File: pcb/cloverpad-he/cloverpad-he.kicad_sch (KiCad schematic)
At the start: 65 parts, among them J1 USB_C_Receptacle_USB2.0, SW1 SW_Push, SW2 SW_Push, U1 SRV05-4, U2 XC6206P332MR, U3 DRV5056A4xDBZxQ1, U4 DRV5056A4xDBZxQ1, U5 DRV5056A4xDBZxQ1, U6 74AHCT1G125, U7 74AHCT1G125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

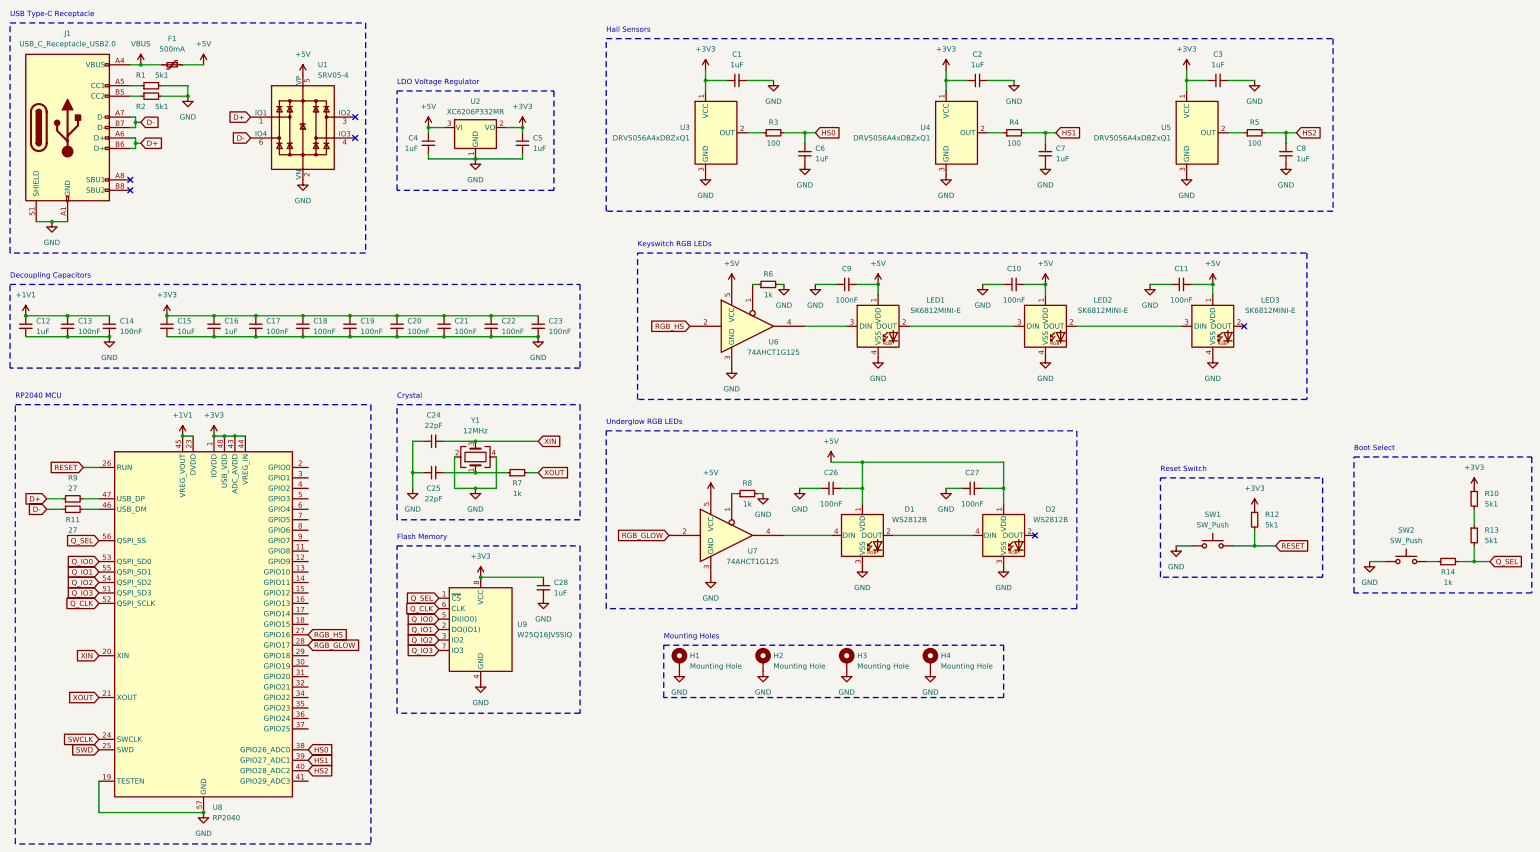
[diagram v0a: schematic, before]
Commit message: chore: remove rgb from Cloverpad HE pcb
I want to keep the cost down; including RGB means that standard PCB assembly is needed, which causes the price to spike...
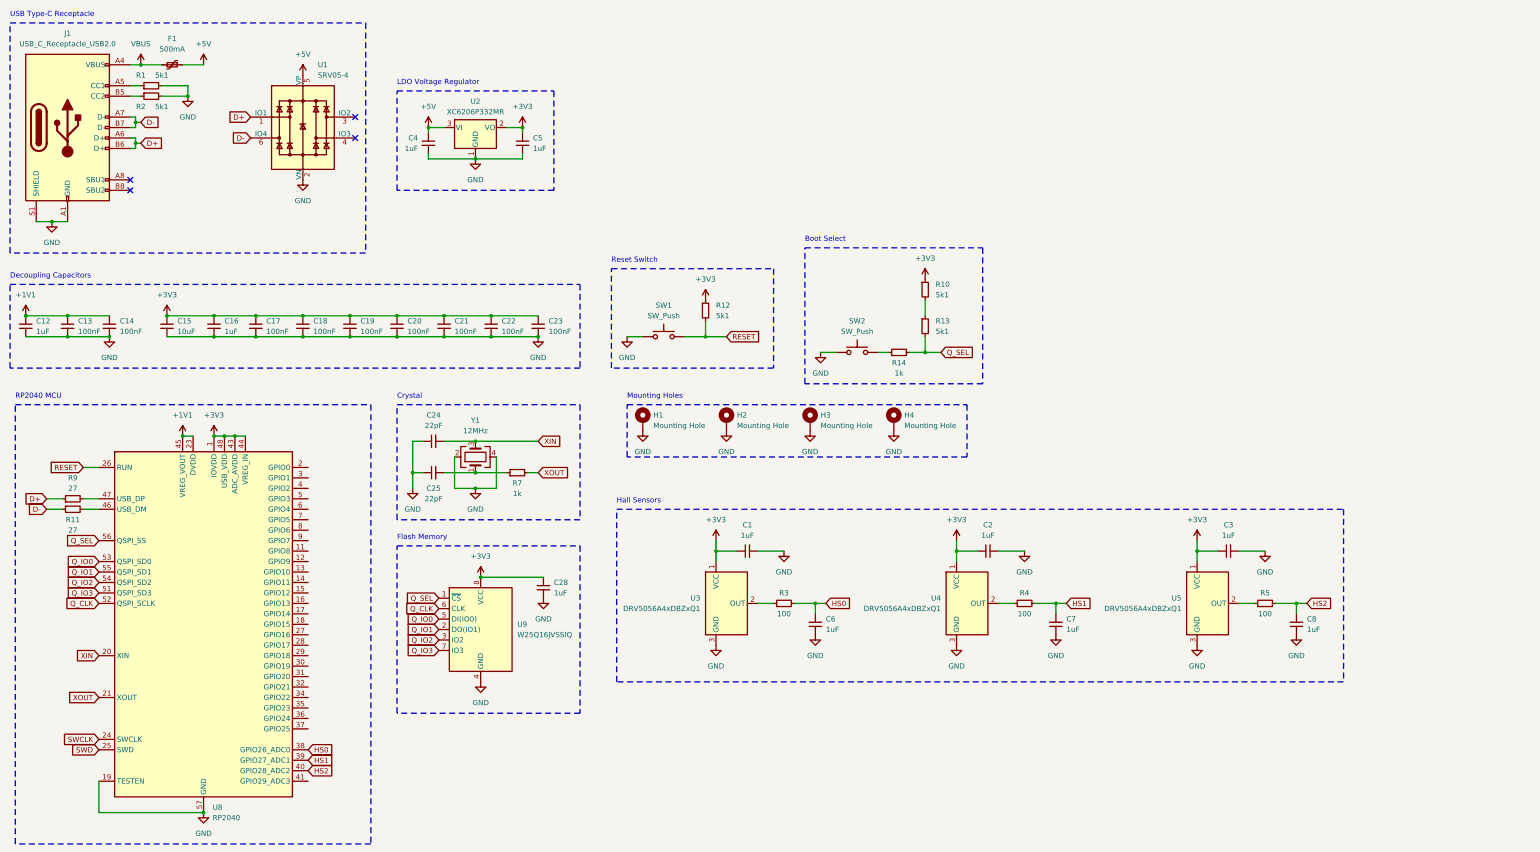
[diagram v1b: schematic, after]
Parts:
- removed C10, C11, C26, C27, C9: 100nF, Capacitor_SMD:C_0402_1005Metric, symbol Device:C_Small
- removed D1, D2: WS2812B, LED_SMD:LED_WS2812B_PLCC4_5.0x5.0mm_P3.2mm, symbol LED:WS2812B
- removed LED1, LED2, LED3: SK6812MINI-E, PCM_marbastlib-mx:LED_MX_6028R, symbol PCM_marbastlib-mx:MX_SK6812MINI-E
- removed R6, R8: 1k, Resistor_SMD:R_0402_1005Metric, symbol Device:R_Small
- removed U6, U7: 74AHCT1G125, Package_TO_SOT_SMD:SOT-353_SC-70-5, symbol 74xGxx:74AHCT1G125
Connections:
- net RGB_GLOW: no longer names the net of U8.28 (GPIO17)
- net RGB_HS: no longer names the net of U8.27 (GPIO16)
- no-connect marks 6 -> 4
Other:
- note removed: "Keyswitch RGB LEDs"
- note removed: "Underglow RGB LEDs"
- moved on the sheet: C1, C2, C3, C6, C7, C8, H1, H2, H3, H4, R10, R12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

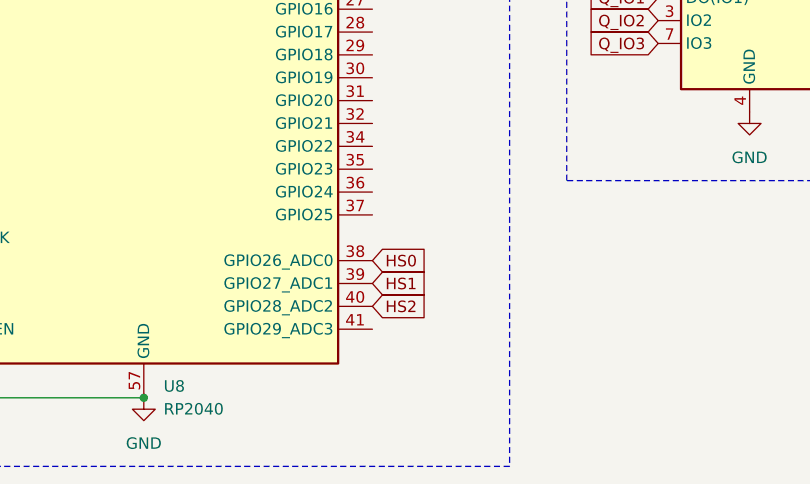
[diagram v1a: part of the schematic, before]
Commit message: fix: swap positions of HS0 and HS2 on cloverpad he
same as on cloverpad mx - this puts HS0 on the leftmost side.
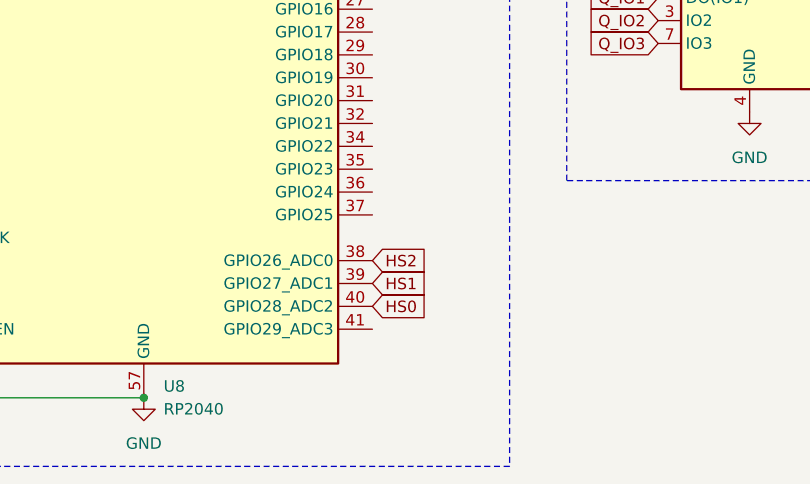
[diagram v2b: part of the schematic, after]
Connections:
- net HS0: now also U8.40 (GPIO28_ADC2); no longer U8.38 (GPIO26_ADC0)
- net HS2: now also U8.38 (GPIO26_ADC0); no longer U8.40 (GPIO28_ADC2)
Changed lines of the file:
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@@
     )
   )
-  (global_label "HS2" (shape input) (at 87.63 199.39 0) (fields_autoplaced)
+  (global_label "HS2" (shape input) (at 87.63 194.31 0) (fields_autoplaced)
     (effects (font (size 1.27 1.27)) (justify left))
-    (property "Intersheetrefs" "${INTERSHEET_REFS}" (at 94.3647 199.39 0)
+    (property "Intersheetrefs" "${INTERSHEET_REFS}" (at 94.3647 194.31 0)
       (effects (font (size 1.27 1.27)) (justify left) hide)
     )
@@
     )
   )
-  (global_label "HS0" (shape input) (at 87.63 194.31 0) (fields_autoplaced)
+  (global_label "HS0" (shape input) (at 87.63 199.39 0) (fields_autoplaced)
     (effects (font (size 1.27 1.27)) (justify left))
-    (property "Intersheetrefs" "${INTERSHEET_REFS}" (at 94.3647 194.31 0)
+    (property "Intersheetrefs" "${INTERSHEET_REFS}" (at 94.3647 199.39 0)
       (effects (font (size 1.27 1.27)) (justify left) hide)
     )

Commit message: fix: port pcb size changes to cloverpad he
since there's no RGB now, it's possible to route the analog signals more directly.
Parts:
- H1, H2, H3, H4: footprint MountingHole:MountingHole_3.5mm_Pad -> MountingHole:MountingHole_2.2mm_M2_Pad
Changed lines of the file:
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@@
       (effects (font (size 1.27 1.27)) (justify left))
     )
-    (property "Footprint" "MountingHole:MountingHole_3.5mm_Pad" (at 189.23 114.3 0)
+    (property "Footprint" "MountingHole:MountingHole_2.2mm_M2_Pad" (at 189.23 114.3 0)
       (effects (font (size 1.27 1.27)) hide)
     )
@@
       (effects (font (size 1.27 1.27)) (justify left))
     )
-    (property "Footprint" "MountingHole:MountingHole_3.5mm_Pad" (at 209.55 114.3 0)
+    (property "Footprint" "MountingHole:MountingHole_2.2mm_M2_Pad" (at 209.55 114.3 0)
       (effects (font (size 1.27 1.27)) hide)
     )
@@
       (effects (font (size 1.27 1.27)) (justify left))
     )
-    (property "Footprint" "MountingHole:MountingHole_3.5mm_Pad" (at 168.91 114.3 0)
+    (property "Footprint" "MountingHole:MountingHole_2.2mm_M2_Pad" (at 168.91 114.3 0)
       (effects (font (size 1.27 1.27)) hide)
     )
@@
       (effects (font (size 1.27 1.27)) (justify left))
     )
-    (property "Footprint" "MountingHole:MountingHole_3.5mm_Pad" (at 229.87 114.3 0)
-      (effects (font (size 1.27 1.27)) hide)
-    )
+    (property "Footprint" "MountingHole:MountingHole_2.2mm_M2_Pad" (at 229.87 114.3 0)
+      (effects (font (size 1.27 1.27)) hide)
+    )
